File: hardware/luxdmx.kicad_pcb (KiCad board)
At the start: 4 copper layers, 99 x 79 mm, 93 parts, among them J1 XLR-5 NC5FAH, J2 USB-C, J3 HY931147C, J4 DISP SH9, J5 XLR-5 NC5FAH, J6 EXP SH9, J7 DMX-OUT A, J8 DMX-OUT B, Q1 MMBT3904, Q2 MMBT3904, SW1 BOOT, SW2 RST, U1 ESP32-S3-WROOM-1-N8, U2 W5500, U3 CH340C, U4 SY8089, U5 ISO3086DWR, U6 ISO3086DWR, U7 DP9900M-5V, U8 USBLC6-2SC6, U9 TPS2116DRLR, Y1 25MHz

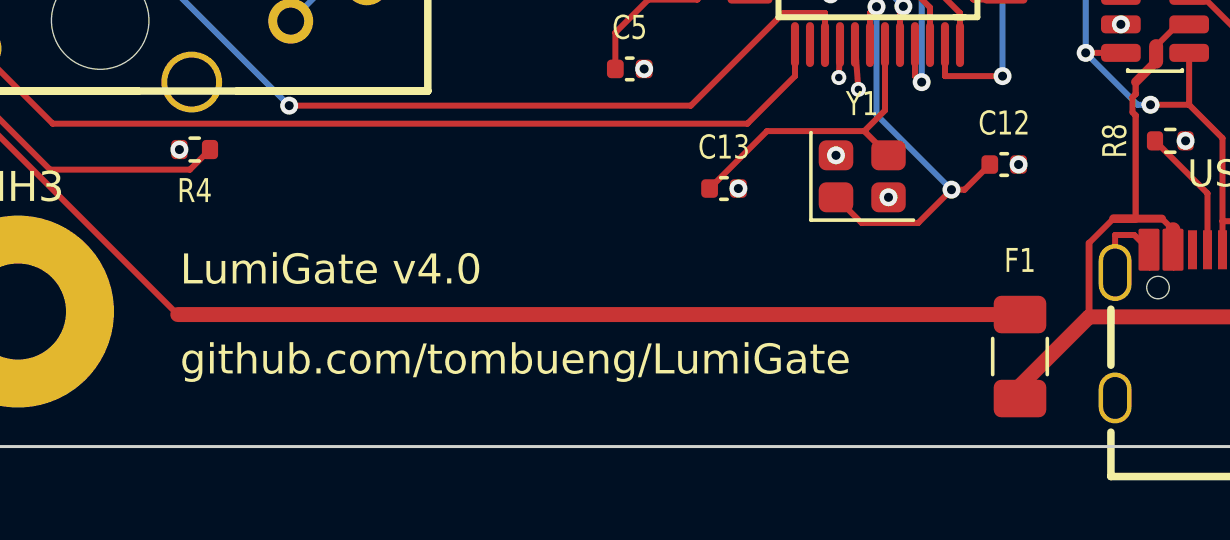
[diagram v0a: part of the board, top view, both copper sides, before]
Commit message: rebrand(hardware): Update PCB silk - LumiGate → LuxDMX + luxdmx.org
Updated all silk text and metadata on the board:
- Title block: LumiGate → LuxDMX
- Company field: github.com/tombueng/LumiGate → luxdmx.org
- F.SilkS line 1: LumiGate v4.0 → LuxDMX v4.0
- F.SilkS line 2: github.com/tombueng/LumiGate → luxdmx.org
- B.SilkS (key features): LumiGate v4 → LuxDMX v4

PCB now displays correct branding and URL when manufactured.
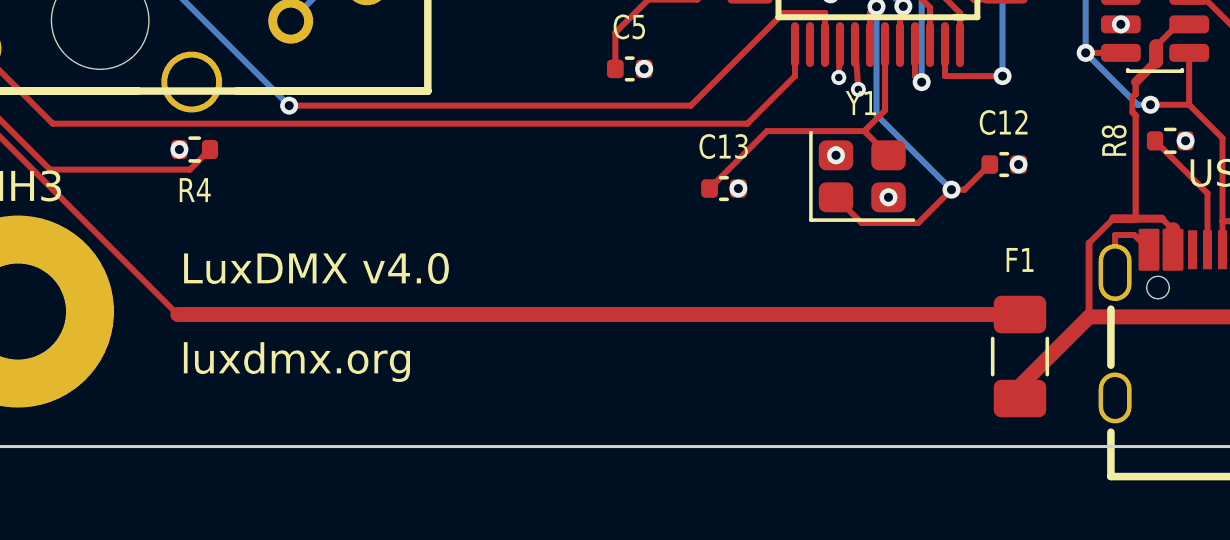
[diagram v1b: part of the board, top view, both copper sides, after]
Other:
- board text added: "LuxDMX v4 -- KEY FEATURES"
- board text added: "LuxDMX v4.0"
- board text added: "luxdmx.org"
- board text removed: "LumiGate v4 -- KEY FEATURES"
- board text removed: "LumiGate v4.0"
- board text removed: "github.com/tombueng/LumiGate"
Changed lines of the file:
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@@
 	(paper "A4")
 	(title_block
-		(title "LumiGate")
+		(title "LuxDMX")
 		(rev "v4.0")
-		(company "github.com/tombueng/LumiGate")
+		(company "luxdmx.org")
 	)
 	(layers
@@
 		)
 	)
-	(gr_text "LumiGate v4.0"
+	(gr_text "LuxDMX v4.0"
 		(at 107.5 162 0)
 		(layer "F.SilkS")
@@
 		)
 	)
-	(gr_text "github.com/tombueng/LumiGate"
+	(gr_text "luxdmx.org"
 		(at 107.5 165 0)
 		(layer "F.SilkS")
@@
 		)
 	)
-	(gr_text "LumiGate v4 -- KEY FEATURES"
+	(gr_text "LuxDMX v4 -- KEY FEATURES"
 		(at 134.5 135.4 0)
 		(layer "B.SilkS")

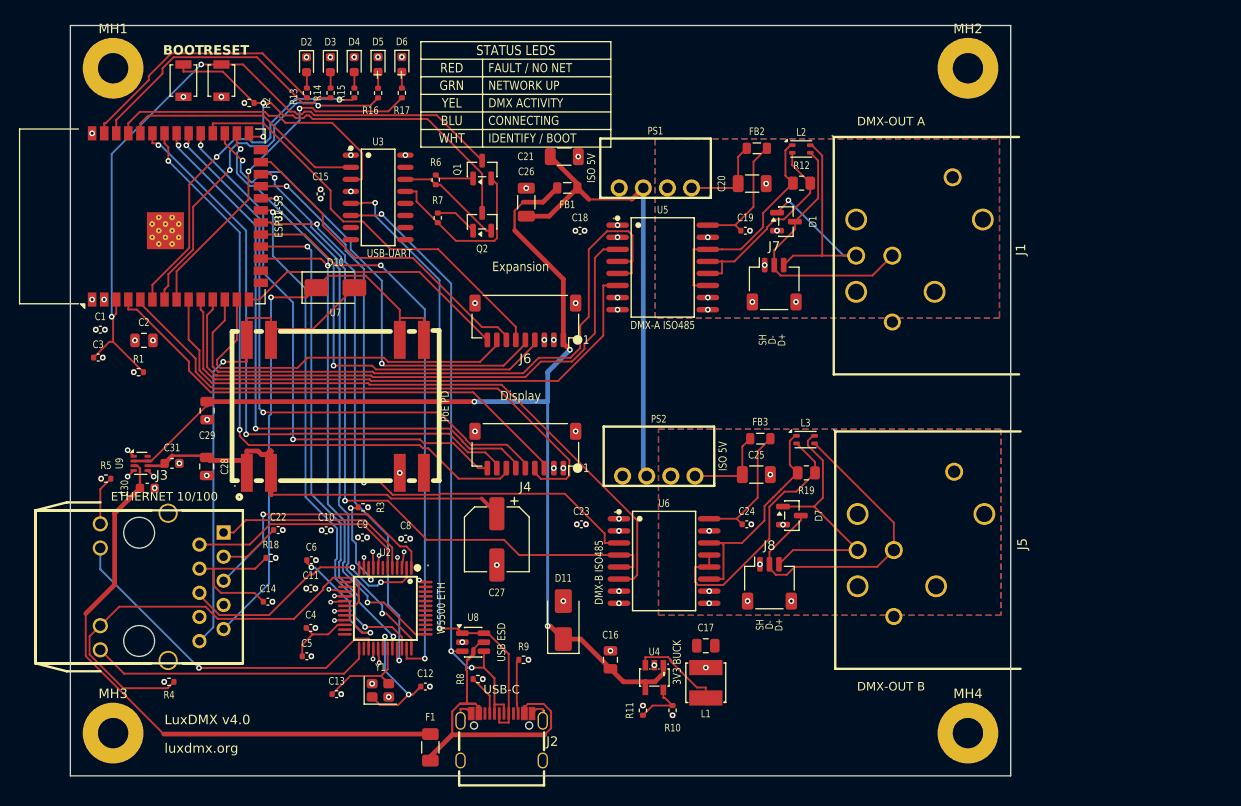
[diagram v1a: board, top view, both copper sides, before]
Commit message: hw: v5.00, DMX512-A "Protected" outputs via series TBU
Swap the series PTCs on each DMX data line for Bourns TBU-CA065-200-WH
high-speed protectors so both outputs meet ANSI E1.11 Annex C "Protected":
they survive a sustained 30 VAC / +-42 VDC fault on the XLR pins. The TBU
triggers in under 1 us and blocks the fault (650 V standoff), so the SM712
only has to eat the sub-us transient.

The 6.5x4mm TBU needs 4mm creepage to board GND, which fought the corner
mounting holes, so the board grew 20mm to the right (now 119x79mm). All four
mounting holes stay on the GND plane and every data net keeps its 4mm
isolation. Re-placed and fully re-routed: 0 unconnected, DRC clean apart
from the 3 known waivable near-misses.

Regenerated from the SKiDL source: netlist, PCB, schematic, symbols, BOM,
CPL, gerbers and the 3D/PCB renders. Silk reads "2x DMX512-A Protected" and
the rev is v5.00 everywhere (hw_version.py stays the single source).

Also drops a pile of one-off hardware scripts from git. Kept the design
source, the reproducible pipeline, the silk/feature steps and the validation
gates; the rest were scratch and are now gitignored.
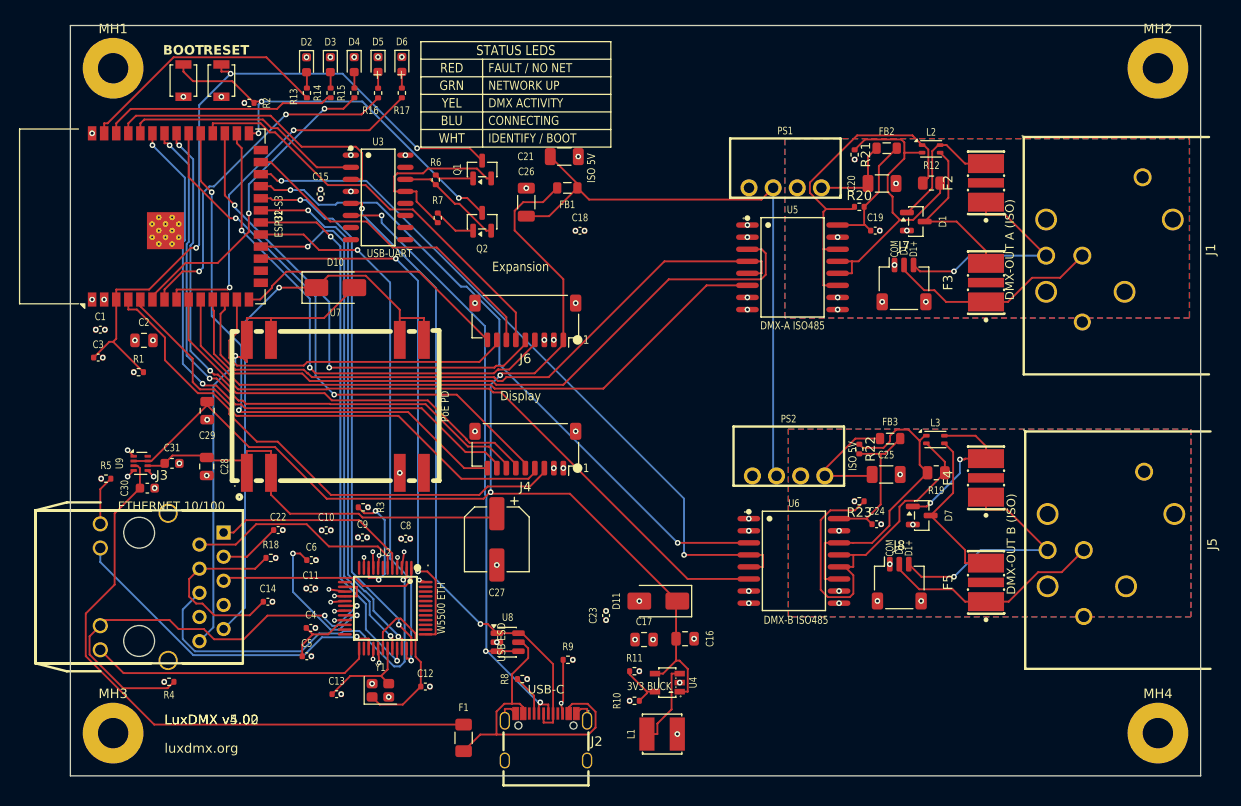
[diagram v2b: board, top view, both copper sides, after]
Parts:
- added F2: TBU 200mA 650V, DIO-SMD_3P-L6.5-W4.0-BI, F.Cu at (194.0, 105.5)
- added F3: TBU 200mA 650V, DIO-SMD_3P-L6.5-W4.0-BI, F.Cu at (194.0, 116.0)
- added F4: TBU 200mA 650V, DIO-SMD_3P-L6.5-W4.0-BI, F.Cu at (194.0, 136.5)
- added F5: TBU 200mA 650V, DIO-SMD_3P-L6.5-W4.0-BI, F.Cu at (194.0, 147.5)
- added R20: 470R, R_0402_1005Metric, F.Cu at (180.7, 108.0)
- added R21: 470R, R_0402_1005Metric, F.Cu at (180.2, 102.5)
- added R22: 470R, R_0402_1005Metric, F.Cu at (180.7, 133.5)
- added R23: 470R, R_0402_1005Metric, F.Cu at (180.7, 139.0)
- moved J1 20.0 mm to (207.0, 112.5)
- moved J5 20.0 mm to (207.2, 143.5)
- moved MH2 20.0 mm to (212.1, 93.4)
- moved MH4 20.0 mm to (212.1, 163.4)
- moved C19 13.7 mm to (182.3, 110.5)
- moved C20 13.7 mm to (183.1, 105.5)
- moved C25 13.7 mm to (183.5, 136.2)
- moved FB3 13.7 mm to (183.9, 132.4)
- moved J7 13.7 mm to (185.4, 116.1)
- moved J8 13.7 mm to (184.9, 147.6)
- moved PS1 13.7 mm to (172.9, 106.0)
- moved U6 13.7 mm to (173.8, 145.3)
- moved C24 13.7 mm to (182.5, 141.4)
- moved D1 13.7 mm to (186.6, 109.5)
- moved D7 13.7 mm to (187.2, 140.5)
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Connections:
- J1 pad 2: DMX_BO -> DMX_BX
- J1 pad 3: DMX_AO -> DMX_AX
- J5 pad 2: DMX2_BO -> DMX2_BX
- J5 pad 3: DMX2_AO -> DMX2_AX
- J7 pad 2: DMX_BO -> DMX_BX
- J7 pad 3: DMX_AO -> DMX_AX
- J8 pad 2: DMX2_BO -> DMX2_BX
- J8 pad 3: DMX2_AO -> DMX2_AX
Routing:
- net DMX2_AX: track 0.00 -> 25.9 mm, vias 0 -> 1
- net DMX_AX: track 0.00 -> 24.3 mm, vias 0 -> 1
- net DMX2_BX: track 0.00 -> 23.6 mm
- net DMX_BX: track 0.00 -> 22.7 mm
- net DMX2_BO: track 36.1 -> 17.7 mm
- net DMX_AO: track 31.6 -> 14.4 mm, vias 1 -> 0
- net ETH_TXP: track 27.3 -> 42.4 mm, vias 2 -> 1
- net DMX2_B: track 27.9 -> 42.1 mm
- net +5V_DMX: track 49.5 -> 63.2 mm
- net DMX_B: track 21.7 -> 34.7 mm
- net DMX_RX: track 61.6 -> 74.4 mm
- net DMX_A: track 24.3 -> 36.6 mm
- net DMX2_AO: track 27.6 -> 16.8 mm, vias 0 -> 2
- net DMX_BO: track 28.1 -> 17.7 mm
- net DMX_TX: track 58.8 -> 68.8 mm
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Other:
- board size 99 x 79 mm -> 119 x 79 mm
- board text added: "2x DMX512-A Protected"
- board text added: "COM"
- board text added: "D1+"
- board text added: "D1-"
- board text added: "DMX-OUT A (ISO)"
- board text added: "DMX-OUT B (ISO)"
- board text added: "LuxDMX v4.02"
- board text added: "LuxDMX v5.00"
- board text added: "LuxDMX v5.00 -- KEY FEATURES"
- board text removed: "2x isolated DMX512-A"
- board text removed: "D+"
- board text removed: "D-"
- board text removed: "DMX-OUT A"
- board text removed: "DMX-OUT B"
- board text removed: "LuxDMX v4 -- KEY FEATURES"
- board text removed: "LuxDMX v4.0"
- board text removed: "SH"

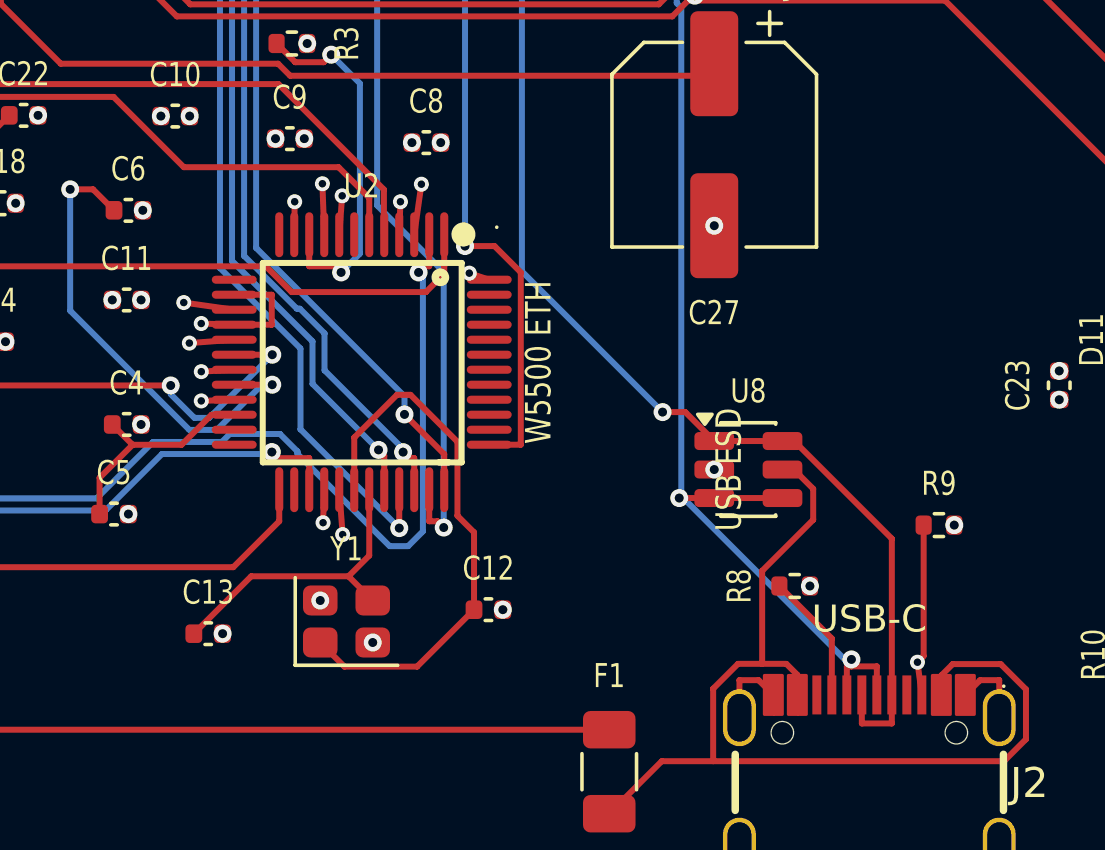
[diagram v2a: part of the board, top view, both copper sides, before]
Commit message: hw: post-validation hardening (vias, fine-pitch clearance, stackup)
Live re-validation after the v5 board turned up real items. Fixed the safe
ones, documented the rest. Every edit was clearance-checked by DRC and the
board was never left worse than the prior step.

- 14 escape vias were 0.125mm annular, under the 0.13mm DFM rule. Re-drilled
  0.25 -> 0.20mm with the pad unchanged, so annular is 0.150mm now with zero
  clearance change. Also removed a stray dangling via on CC2.
- The 3 W5500/USB-C clearance "errors" were fine-pitch escapes (0.16-0.174mm)
  that cannot reach 0.2mm at a 0.5mm QFN pitch (the pad geometry forbids it).
  Set the Default netclass clearance to a realistic 0.15mm, still 68% over
  JLC's 0.089mm minimum. No copper moved. DRC clearance errors now 0.
- Added the JLC04161H-7628 4-layer stackup so impedance is defined. With the
  0.2mm traces the Ethernet pairs land around 117 ohm differential (target is
  100) and are not actually coupled (ETH_TXP takes a 42mm B.Cu detour vs
  ETH_TXN's 22mm F.Cu). Left the Ethernet re-route for a supervised GUI pass
  rather than scripting it blind; it works for short 100BASE-TX as is.
  Documented in VALIDATION.md.

Final: 0 unrouted, 0 schematic-parity, 0 DRC errors, 62 cosmetic silk warnings
(the fab auto-clips silk off pads and edges). Gerbers regenerated. Still a
first-spin prototype, never fabricated.
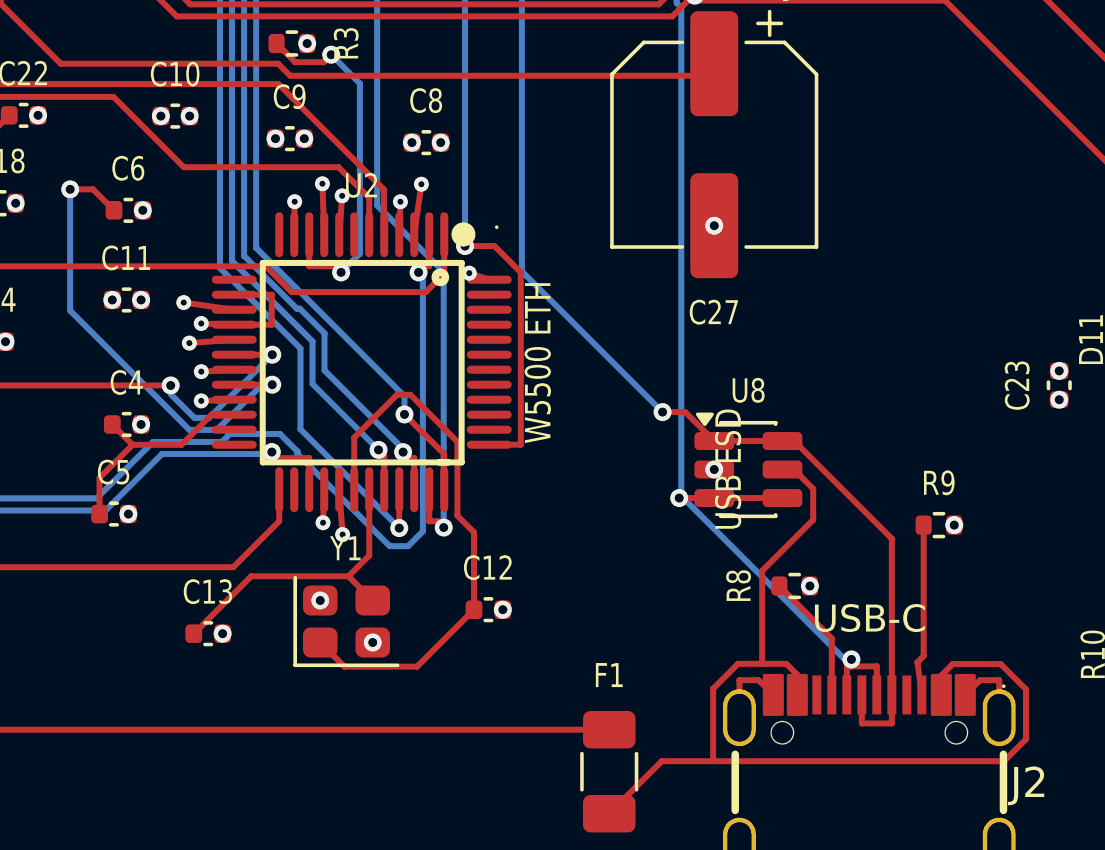
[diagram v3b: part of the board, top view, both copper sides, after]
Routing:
- net CC2: vias 1 -> 0
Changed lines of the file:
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@@
 	)
 	(setup
+		(stackup
+			(layer "F.SilkS" (type "Top Silk Screen"))
+			(layer "F.Paste" (type "Top Solder Paste"))
+			(layer "F.Mask" (type "Top Solder Mask") (thickness 0.0152))
+			(layer "F.Cu" (type "copper") (thickness 0.035))
+			(layer "dielectric 1" (type "prepreg") (thickness 0.2104) (material "7628") (epsilon_r 4.05) (loss_tangent 0.0182))
+			(layer "In1.Cu" (type "copper") (thickness 0.0152))
+			(layer "dielectric 2" (type "core") (thickness 1.065) (material "FR4") (epsilon_r 4.6) (loss_tangent 0.02))
+			(layer "In2.Cu" (type "copper") (thickness 0.0152))
+			(layer "dielectric 3" (type "prepreg") (thickness 0.2104) (material "7628") (epsilon_r 4.05) (loss_tangent 0.0182))
+			(layer "B.Cu" (type "copper") (thickness 0.035))
+			(layer "B.Mask" (type "Bottom Solder Mask") (thickness 0.0152))
+			(layer "B.Paste" (type "Bottom Solder Paste"))
+			(layer "B.SilkS" (type "Bottom Silk Screen"))
+			(copper_finish "ENIG")
+			(dielectric_constraints no)
+		)
 		(pad_to_mask_clearance 0)
 		(allow_soldermask_bridges_in_footprints no)
@@
 		(at 125.400714 148.960352)
 		(size 0.5)
-		(drill 0.25)
+		(drill 0.2)
 		(layers "F.Cu" "B.Cu")
 		(locked yes)
@@
 		(at 132.738245 144.316777)
 		(size 0.5)
-		(drill 0.25)
+		(drill 0.2)
 		(layers "F.Cu" "B.Cu")
 		(locked yes)
@@
 		(at 130.112884 155.995746)
 		(size 0.5)
-		(drill 0.25)
+		(drill 0.2)
 		(layers "F.Cu" "B.Cu")
 		(locked yes)
@@
 		(at 129.438725 144.301104)
 		(size 0.5)
-		(drill 0.25)
+		(drill 0.2)
 		(layers "F.Cu" "B.Cu")
 		(locked yes)
@@
 		(at 134.33494 147.281606)
 		(size 0.5)
-		(drill 0.25)
+		(drill 0.2)
 		(layers "F.Cu" "B.Cu")
 		(locked yes)
@@
 		(at 125.401898 150.564594)
 		(size 0.5)
-		(drill 0.25)
+		(drill 0.2)
 		(layers "F.Cu" "B.Cu")
 		(locked yes)
@@
 		(at 128.51441 144.900094)
 		(size 0.5)
-		(drill 0.25)
+		(drill 0.2)
 		(layers "F.Cu" "B.Cu")
 		(locked yes)
@@
 		(at 130.097833 144.703686)
 		(size 0.5)
-		(drill 0.25)
+		(drill 0.2)
 		(layers "F.Cu" "B.Cu")
 		(locked yes)
@@
 		(at 125.400714 151.539647)
 		(size 0.5)
-		(drill 0.25)
+		(drill 0.2)
 		(layers "F.Cu" "B.Cu")
 		(locked yes)
@@
 		(at 129.460352 155.599285)
 		(size 0.5)
-		(drill 0.25)
+		(drill 0.2)
 		(layers "F.Cu" "B.Cu")
 		(locked yes)
@@
 		(at 132.039647 144.900714)
 		(size 0.5)
-		(drill 0.25)
+		(drill 0.2)
 		(layers "F.Cu" "B.Cu")
 		(locked yes)
@@
 		(at 125.004253 149.612884)
 		(size 0.5)
-		(drill 0.25)
+		(drill 0.2)
 		(layers "F.Cu" "B.Cu")
 		(locked yes)
@@
 		(at 124.816777 148.261754)
 		(size 0.5)
-		(drill 0.25)
+		(drill 0.2)
 		(layers "F.Cu" "B.Cu")
 		(locked yes)
@@
 		(net "CC2")
 	)
-	(via
-		(at 149.273486 160.2498)
-		(size 0.5)
-		(drill 0.25)
-		(layers "F.Cu" "B.Cu")
-		(locked yes)
-		(net "CC2")
-	)
